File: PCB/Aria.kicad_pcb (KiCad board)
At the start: 4 copper layers, 29 x 78 mm, 85 parts, among them J1 B2B-PH-K-S(LF)(SN), J2 B3B-PH-K-S(LF)(SN), J3 20021121-00010C4LF, J4 0475890001-MicroUSBPort, P1 CONN_01X18, P2 CONN_01X18, Q1 DMG2307L-7, Q2 DMG2307L-7, SW1 B3U-1000P, SW2 B3U-1000P, T1 1909763-1, U1 BQ24210DQCT, U2 AZ1117CR-3.3TRG1_1, U3 STM32F446RET6_-_TQFP64, U4 ESP8285, X1 ABM3B8.000MHZB2T, X2 ABS07-32.768KHZ-9-T, X3 FA-128_26.0000MF10Z-AC3

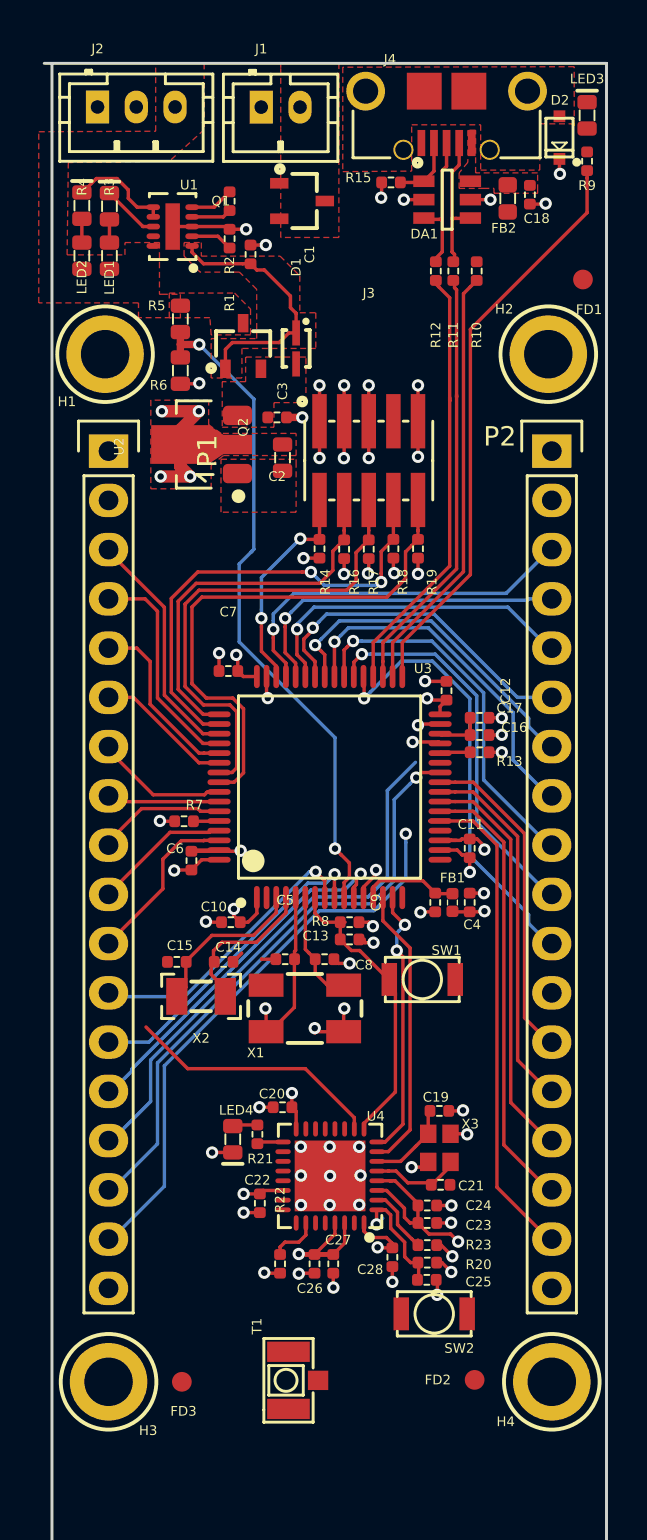
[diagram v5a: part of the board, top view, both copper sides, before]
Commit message: More routing
more routing completed, but thinking of scraping the current pass
entirely and rechoosing all the pins.
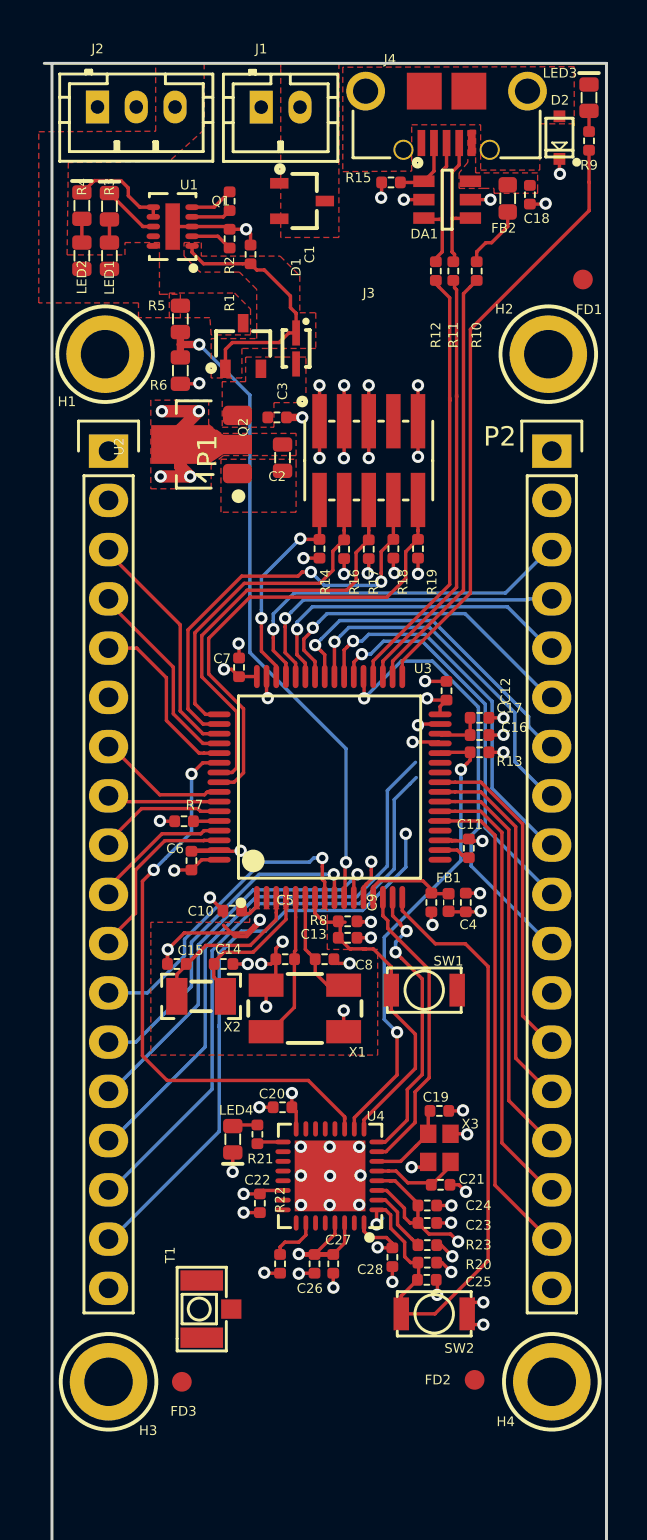
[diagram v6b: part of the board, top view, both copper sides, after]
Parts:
- moved T1 5.79 mm to (62.1, 94.2)
- moved R9 1.05 mm to (82.1, 34.0)
- moved LED3 0.92 mm to (82.1, 31.8)
- moved C10 0.60 mm to (63.7, 73.7)
- moved C7 0.58 mm to (64.0, 61.1), turned to 90 degrees
- moved SW1 0.56 mm to (73.6, 77.8)
- moved C4 0.20 mm to (75.7, 73.3)
- moved C9 0.20 mm to (74.0, 73.3)
- moved FB1 0.20 mm to (74.9, 73.3)
- moved C13 0.13 mm to (69.7, 75.1)
- moved R8 0.11 mm to (69.7, 74.2)
- moved C14 0.11 mm to (63.2, 76.5)
- moved C15 0.11 mm to (60.8, 76.5)
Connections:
- U4 pad 22: /MCU_STM32F446RET6/ESPTOST_BOOT1 -> /MCU_STM32F446RET6/ESPTOST_BOOT0
- U4 pad 23: /MCU_STM32F446RET6/ESPTOST_BOOT0 -> /MCU_STM32F446RET6/ESPTOST_BOOT1
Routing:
- net /MCU_STM32F446RET6/STM_ESP_RST: track 6.19 -> 35.4 mm
- net /MCU_STM32F446RET6/ESPTOST_BOOT1: track 1.57 -> 24.0 mm, vias 0 -> 2
- net GND: track 89.3 -> 105.0 mm, vias 54 -> 60
- net /MCU_STM32F446RET6/ESPTOST_BOOT0: track 20.5 -> 29.7 mm, vias 0 -> 2
- net /MCU_STM32F446RET6/VBUS: track 13.4 -> 16.8 mm
- net /MCU_STM32F446RET6/SWO_TDO: track 25.1 -> 22.1 mm
- net /MCU_STM32F446RET6/NJTRST: track 27.9 -> 24.9 mm
- net /MCU_STM32F446RET6/SWCLK_TCK: track 19.7 -> 17.5 mm
- net /MCU_STM32F446RET6/SWO_TDI: track 24.2 -> 22.0 mm
- net +3V3: track 54.5 -> 52.5 mm, vias 26 -> 25
- net /MCU_STM32F446RET6/ESP_ST_RST: track 14.8 -> 16.6 mm
- net /MCU_STM32F446RET6/PC0: track 15.0 -> 16.5 mm
- net /MCU_STM32F446RET6/PB1: track 29.0 -> 30.5 mm
- net /MCU_STM32F446RET6/PC3: track 19.1 -> 20.6 mm
- net /MCU_STM32F446RET6/PC13: track 27.8 -> 29.2 mm
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
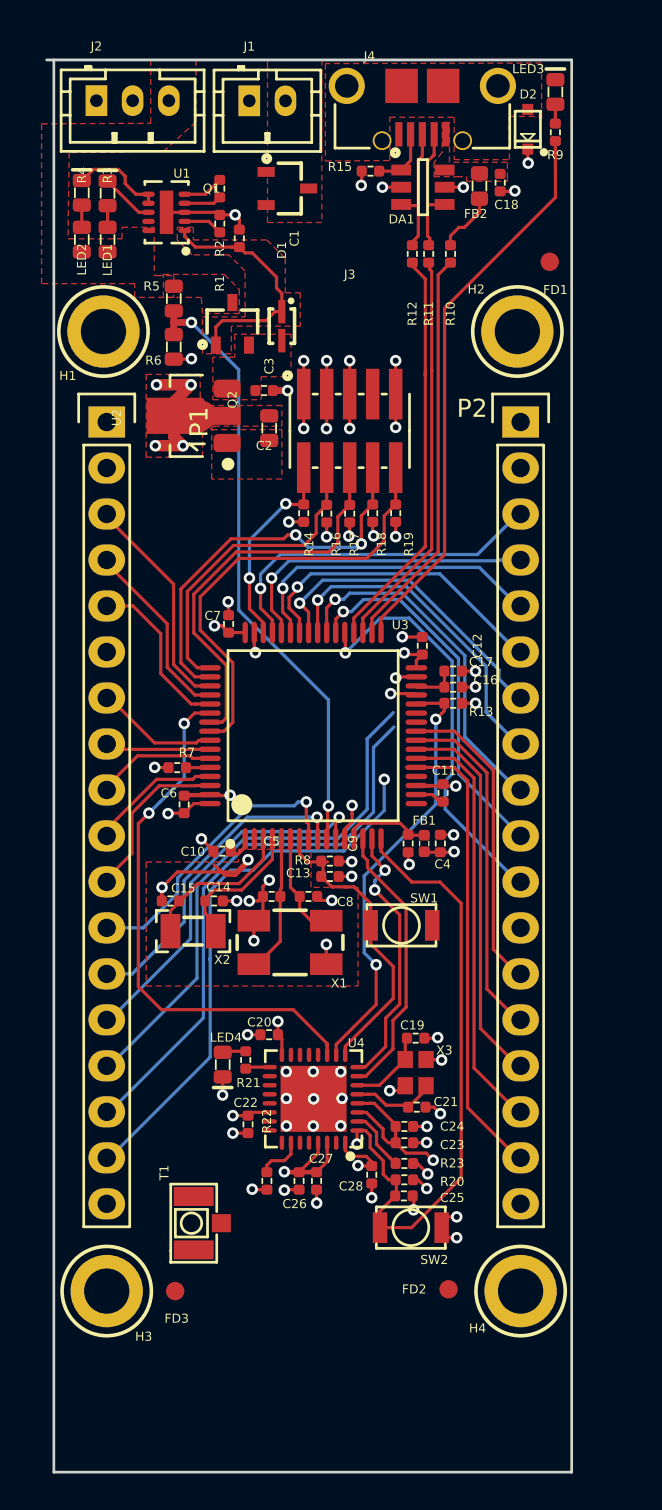
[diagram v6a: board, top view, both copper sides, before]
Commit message: Updates
Changed board size, heavily altered schematic and pinning to be more
efficient. Program mode for ESP8285 is switched to GPIO0 being pulled
high 10k and toggled by STM32. Board at 30mm By 70.5mm. Also switching
to chip antenna next commit, expect updates to libraries.
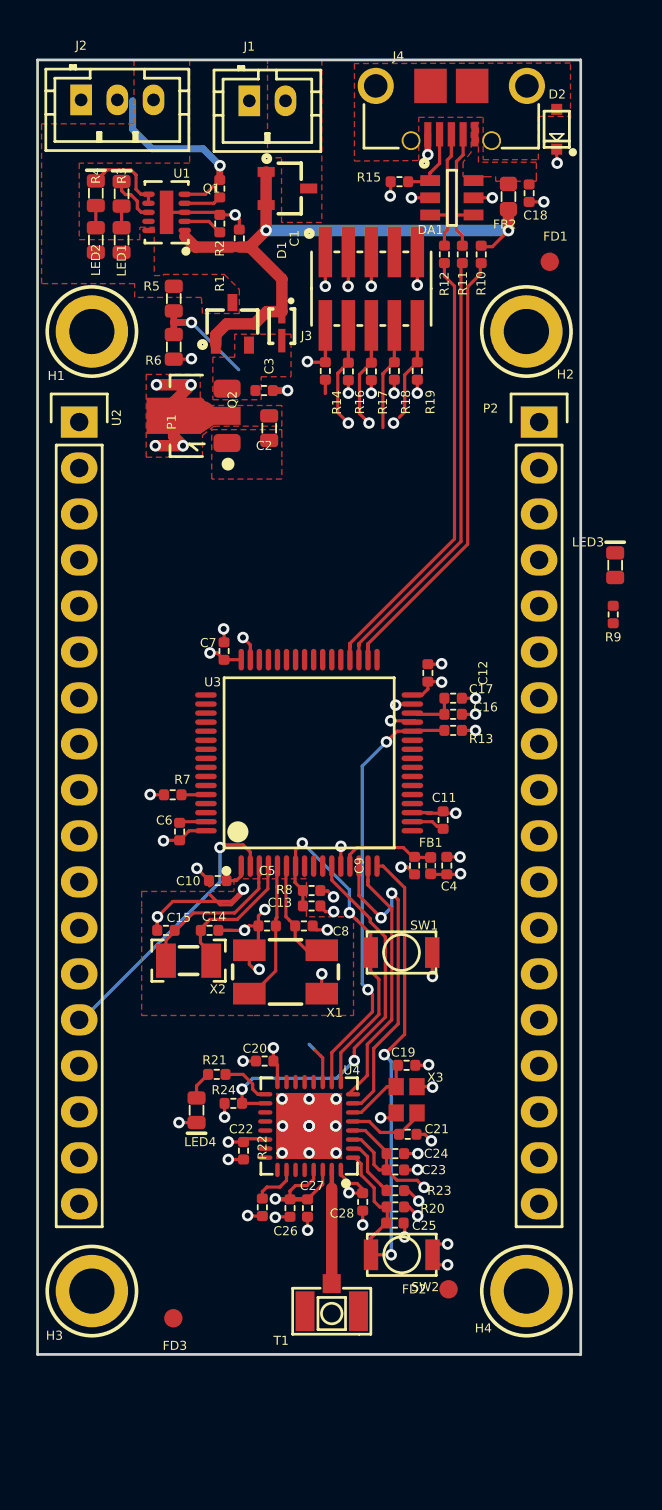
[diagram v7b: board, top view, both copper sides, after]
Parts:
- added R24: RC1005F103CS, PCB_Footprints:R0402, F.Cu at (64.3, 87.6)
- moved R9 26.8 mm to (85.3, 60.6)
- moved LED3 26.3 mm to (85.4, 57.9)
- moved T1 9.04 mm to (69.7, 99.1), turned to 0 degrees
- moved R16 7.94 mm to (70.7, 47.2)
- moved R17 7.94 mm to (71.9, 47.2)
- moved J3 7.94 mm to (71.9, 42.6)
- moved R14 7.94 mm to (69.4, 47.2)
- moved R18 7.94 mm to (73.2, 47.2)
- moved R19 7.94 mm to (74.5, 47.2)
- moved LED4 2.91 mm to (62.3, 88.0)
- moved C13 1.92 mm to (68.6, 76.7)
- moved R8 1.92 mm to (68.6, 75.9)
- moved R11 1.86 mm to (77.0, 40.7)
- moved R21 1.79 mm to (63.4, 86.0), turned to 0 degrees
- moved R12 1.77 mm to (76.0, 40.7)
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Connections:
- P1 pad 10: /MCU_STM32F446RET6/PB8 -> /MCU_STM32F446RET6/PB6
- P1 pad 11: /MCU_STM32F446RET6/PB9 -> /MCU_STM32F446RET6/PB7
- P1 pad 12: /MCU_STM32F446RET6/PC0 -> /MCU_STM32F446RET6/PB8
- P1 pad 13: /MCU_STM32F446RET6/PC1 -> /MCU_STM32F446RET6/PB9
- P1 pad 14: /MCU_STM32F446RET6/PC3 -> /MCU_STM32F446RET6/PC13
- P1 pad 15: /MCU_STM32F446RET6/PC13 -> /MCU_STM32F446RET6/PC0
- P1 pad 16: /MCU_STM32F446RET6/PB0 -> /MCU_STM32F446RET6/PC1
- P1 pad 17: /MCU_STM32F446RET6/PB1 -> /MCU_STM32F446RET6/PC9
- P1 pad 3: /MCU_STM32F446RET6/PC10 -> /MCU_STM32F446RET6/PA10
- P1 pad 4: /MCU_STM32F446RET6/PC11 -> /MCU_STM32F446RET6/PA11
- P1 pad 5: /MCU_STM32F446RET6/PC12 -> /MCU_STM32F446RET6/PA12
- P1 pad 6: /MCU_STM32F446RET6/ESPTOST_BOOT0 -> /MCU_STM32F446RET6/PC10
- P1 pad 7: /MCU_STM32F446RET6/PB5 -> /MCU_STM32F446RET6/PC11
- P1 pad 8: /MCU_STM32F446RET6/PB6 -> /MCU_STM32F446RET6/PC12
- P1 pad 9: /MCU_STM32F446RET6/PB7 -> /MCU_STM32F446RET6/PB5
- P2 pad 10: /MCU_STM32F446RET6/PC7 -> /MCU_STM32F446RET6/PB0
- P2 pad 11: /MCU_STM32F446RET6/PC6 -> /MCU_STM32F446RET6/PC5
- P2 pad 12: /MCU_STM32F446RET6/PB10 -> /MCU_STM32F446RET6/PC4
- P2 pad 13: /MCU_STM32F446RET6/PC5 -> /MCU_STM32F446RET6/PA7
- P2 pad 14: /MCU_STM32F446RET6/PC4 -> /MCU_STM32F446RET6/PA6
- P2 pad 15: /MCU_STM32F446RET6/PA7 -> /MCU_STM32F446RET6/PA5
- P2 pad 16: /MCU_STM32F446RET6/PA6 -> /MCU_STM32F446RET6/PA4
- P2 pad 17: /MCU_STM32F446RET6/PA5 -> /MCU_STM32F446RET6/PA3
- P2 pad 3: /MCU_STM32F446RET6/PA12 -> /MCU_STM32F446RET6/PA9
- P2 pad 4: /MCU_STM32F446RET6/PA11 -> /MCU_STM32F446RET6/PA8
- P2 pad 5: /MCU_STM32F446RET6/PA10 -> /MCU_STM32F446RET6/PC8
- P2 pad 6: /MCU_STM32F446RET6/PA9 -> /MCU_STM32F446RET6/PC7
- P2 pad 7: /MCU_STM32F446RET6/PA8 -> /MCU_STM32F446RET6/PC6
- P2 pad 8: /MCU_STM32F446RET6/PC9 -> /MCU_STM32F446RET6/PB10
- P2 pad 9: /MCU_STM32F446RET6/PC8 -> /MCU_STM32F446RET6/PB1
- U3 pad 11: /MCU_STM32F446RET6/PC3 -> /MCU_STM32F446RET6/ESP_PGM_MODE
- U3 pad 17: /MCU_STM32F446RET6/ESP_PGM_MODE -> /MCU_STM32F446RET6/PA3
- U4 pad 15: Net-(U4-Pad15) -> /MCU_STM32F446RET6/ESP_PGM_MODE
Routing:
- net /MCU_STM32F446RET6/HEARTBEAT: track 31.1 -> 0.00 mm
- net /MCU_STM32F446RET6/PB0: track 31.0 -> 0.00 mm
- net /MCU_STM32F446RET6/PB1: track 30.5 -> 0.00 mm, vias 1 -> 0
- net /MCU_STM32F446RET6/BAT_VOLT: track 34.0 -> 5.97 mm, vias 2 -> 1
- net /MCU_STM32F446RET6/ESPTOST_BOOT0: track 29.7 -> 1.95 mm, vias 2 -> 0
- net /MCU_STM32F446RET6/PA5: track 25.8 -> 0.54 mm
- net /MCU_STM32F446RET6/PA6: track 23.2 -> 0.00 mm
- net /MCU_STM32F446RET6/PC6: track 23.0 -> 0.00 mm, vias 1 -> 0
- net /MCU_STM32F446RET6/ESP_PGM_MODE: track 0.00 -> 21.6 mm, vias 0 -> 2
- net /MCU_STM32F446RET6/PA7: track 21.2 -> 0.00 mm
- net /MCU_STM32F446RET6/PC3: track 20.6 -> 0.00 mm, vias 1 -> 0
- net /MCU_STM32F446RET6/PC7: track 20.6 -> 0.00 mm, vias 1 -> 0
- net /MCU_STM32F446RET6/PC8: track 19.5 -> 0.00 mm, vias 1 -> 0
- net /MCU_STM32F446RET6/NJTRST: track 24.9 -> 5.49 mm
- net /MCU_STM32F446RET6/PA12: track 19.2 -> 0.00 mm, vias 1 -> 0
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- removed copper zone on F.Cu, net /Power/VBUS
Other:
- board size 29 x 78 mm -> 30 x 71.5 mm

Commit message: Board Finished
Board finished
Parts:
- added ANT1: Inverted_F_PCB_Antenna, PCB_Footprints:PCB_IF_ANT_2.4G, F.Cu at (225.3, 72.3)
- added C29: 600L5R6BT200T, PCB_Footprints:C0402, F.Cu at (211.7, 83.2)
- added R25: ERJ-2GE0R00X, PCB_Footprints:R0402, F.Cu at (216.7, 83.2)
- added R26: ERJ-2GE0R00X, PCB_Footprints:R0402, F.Cu at (215.4, 83.6)
- moved H3 157.4 mm to (213.9, 95.6), turned to 90 degrees
- moved FD3 149.6 mm to (210.5, 93.6), turned to 90 degrees
- moved T1 146.1 mm to (215.4, 87.6)
- moved R22 143.2 mm to (209.0, 87.0), turned to 0 degrees
- moved C26 141.8 mm to (209.0, 85.5), turned to 0 degrees
- moved LED4 141.4 mm to (203.6, 90.6), turned to 0 degrees
- moved C22 141.0 mm to (205.9, 88.0), turned to 0 degrees
- moved C27 140.9 mm to (209.0, 84.5), turned to 0 degrees
- moved SW2 139.5 mm to (212.1, 79.3), turned to 270 degrees
- moved R24 138.9 mm to (203.2, 88.6), turned to 90 degrees
- moved R21 138.3 mm to (201.6, 89.5), turned to 90 degrees
- moved C25 137.8 mm to (210.3, 79.8), turned to 90 degrees
- moved C28 137.7 mm to (208.7, 81.4), turned to 0 degrees
- moved R20 136.8 mm to (209.4, 79.8), turned to 90 degrees
- moved U4 136.1 mm to (204.5, 84.4), turned to 180 degrees
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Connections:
- P1 pad 10: /MCU_STM32F446RET6/PB6 -> /MCU_STM32F446RET6/PB5
- P1 pad 11: /MCU_STM32F446RET6/PB7 -> /MCU_STM32F446RET6/PB6
- P1 pad 12: /MCU_STM32F446RET6/PB8 -> /MCU_STM32F446RET6/PB7
- P1 pad 13: /MCU_STM32F446RET6/PB9 -> /MCU_STM32F446RET6/PB8
- P1 pad 14: /MCU_STM32F446RET6/PC13 -> /MCU_STM32F446RET6/PB9
- P1 pad 15: /MCU_STM32F446RET6/PC0 -> /MCU_STM32F446RET6/PC13
- P1 pad 16: /MCU_STM32F446RET6/PC1 -> /MCU_STM32F446RET6/PC0
- P1 pad 17: /MCU_STM32F446RET6/PC9 -> /MCU_STM32F446RET6/PC1
- P1 pad 3: /MCU_STM32F446RET6/PA10 -> /MCU_STM32F446RET6/PA9
- P1 pad 4: /MCU_STM32F446RET6/PA11 -> /MCU_STM32F446RET6/PA10
- P1 pad 5: /MCU_STM32F446RET6/PA12 -> /MCU_STM32F446RET6/PA11
- P1 pad 6: /MCU_STM32F446RET6/PC10 -> /MCU_STM32F446RET6/PA12
- P1 pad 7: /MCU_STM32F446RET6/PC11 -> /MCU_STM32F446RET6/PC10
- P1 pad 8: /MCU_STM32F446RET6/PC12 -> /MCU_STM32F446RET6/PC11
- P1 pad 9: /MCU_STM32F446RET6/PB5 -> /MCU_STM32F446RET6/PC12
- P2 pad 3: /MCU_STM32F446RET6/PA9 -> /MCU_STM32F446RET6/PA8
- P2 pad 4: /MCU_STM32F446RET6/PA8 -> /MCU_STM32F446RET6/PC9
- T1 pad 1: /WiFi-ESP8285/ANTENNA -> /WiFi-ESP8285/ANT_UM
- U4 pad 2: /WiFi-ESP8285/ANTENNA -> /WiFi-ESP8285/LNA
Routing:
- net GND: track 91.6 -> 131.0 mm, vias 58 -> 82
- net /MCU_STM32F446RET6/BAT_VOLT: track 5.97 -> 37.4 mm, vias 1 -> 2
- net /MCU_STM32F446RET6/ESPTOST_BOOT0: track 1.95 -> 26.2 mm, vias 0 -> 2
- net /MCU_STM32F446RET6/PC1: track 0.00 -> 23.4 mm, vias 0 -> 1
- net /MCU_STM32F446RET6/PA3: track 0.00 -> 22.4 mm, vias 0 -> 1
- net /MCU_STM32F446RET6/PA4: track 0.00 -> 21.3 mm, vias 0 -> 1
- net /MCU_STM32F446RET6/PC0: track 0.00 -> 21.3 mm, vias 0 -> 1
- net /MCU_STM32F446RET6/NJTRST: track 5.49 -> 26.4 mm, vias 0 -> 2
- net /MCU_STM32F446RET6/PA5: track 0.54 -> 21.0 mm, vias 0 -> 1
- net /MCU_STM32F446RET6/PC6: track 0.00 -> 19.4 mm, vias 0 -> 1
- net /MCU_STM32F446RET6/SWO_TDO: track 5.88 -> 25.1 mm, vias 1 -> 2
- net /MCU_STM32F446RET6/PA6: track 0.00 -> 18.6 mm, vias 0 -> 1
- net /MCU_STM32F446RET6/PC7: track 0.00 -> 18.4 mm, vias 0 -> 1
- net /MCU_STM32F446RET6/SWO_TDI: track 5.90 -> 23.5 mm, vias 0 -> 2
- net /MCU_STM32F446RET6/PC8: track 0.00 -> 17.2 mm, vias 0 -> 1
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- added copper zone on B.Cu, net /Power/BAT
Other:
- board size 30 x 71.5 mm -> 80 x 27 mm
- board text added: "Aria 0.1a"
- board text added: "GND 3V3 PA8 PC9 PC8 PC7 PC6 PB10 PB1 PB0 PC5 PC4 PA7 PA6 PA5 PA4 PA3 GND"
- board text added: "GND 3V3 PA9 PA10 PA11 PA12 PC10 PC11 PC12 PB5 PB6 PB7 PB8 PB9 PC13 PC0 PC1 GND"
- board text added: "GND SOLAR V+"
- board text added: "GND THERM BATTERY"
- board text added: "Solar+WiFi Dev Kit https://github.com/adamjvr/Aria"
- board text added: "adamjvr"
